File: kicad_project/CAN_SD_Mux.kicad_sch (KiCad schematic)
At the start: 5 parts, among them U24 SN74CB3Q3257PWR

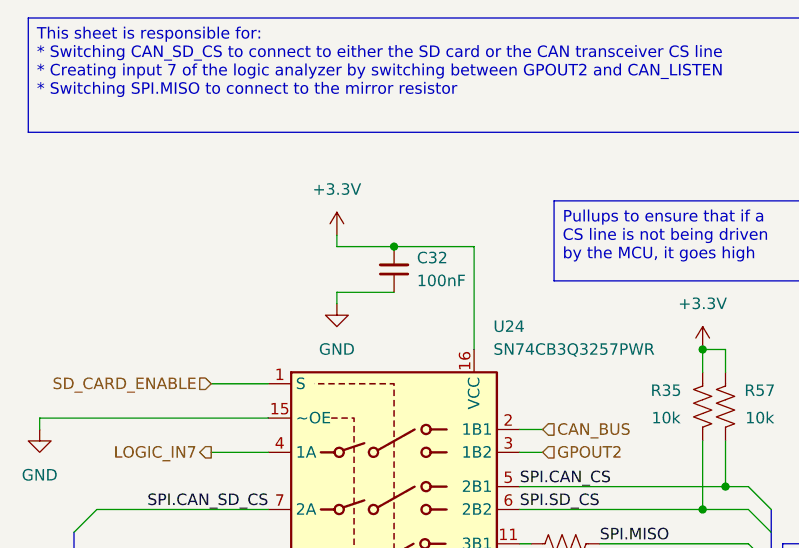
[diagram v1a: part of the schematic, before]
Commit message: Finish schematic and placement for all remaining RP2354 power passives
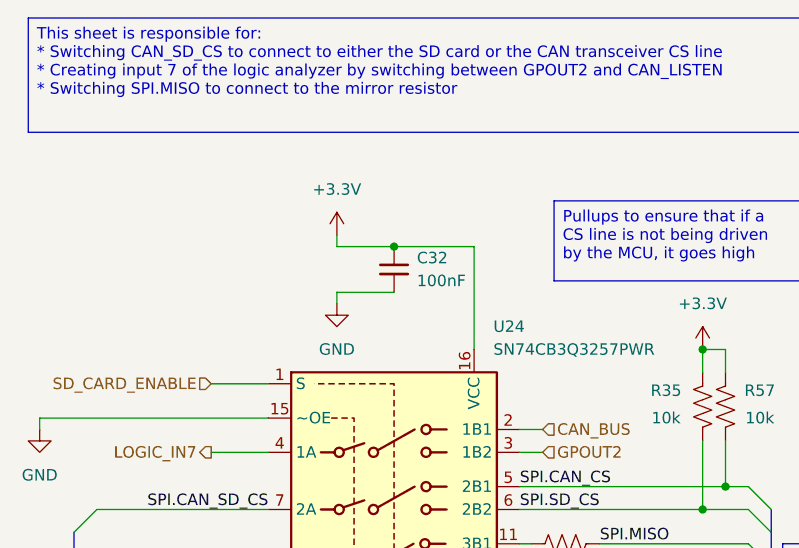
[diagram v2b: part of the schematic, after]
